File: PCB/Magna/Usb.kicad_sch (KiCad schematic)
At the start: 32 parts, among them J801 USB_A, J802 USB_C_Receptacle_USB2.0, J803 USB_B, U801 SRV05-4, U802 USB3300-EZK

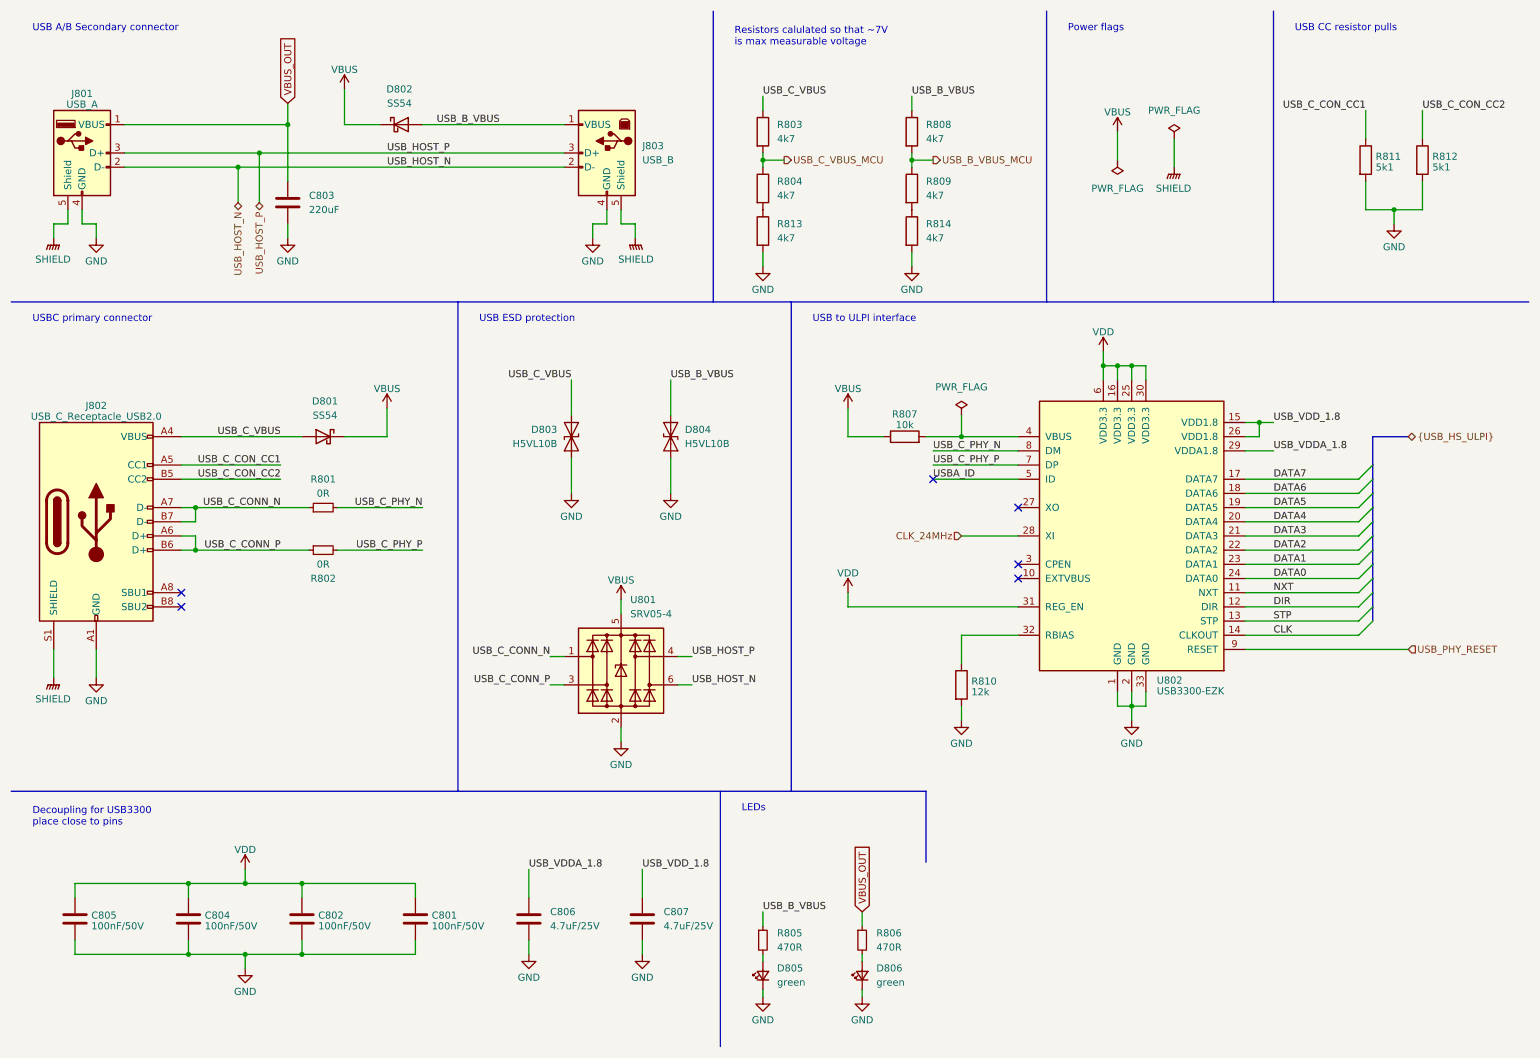
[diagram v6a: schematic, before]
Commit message: Split schematic to several projects
To allow for several boards to be done a kicad project
is needed for each
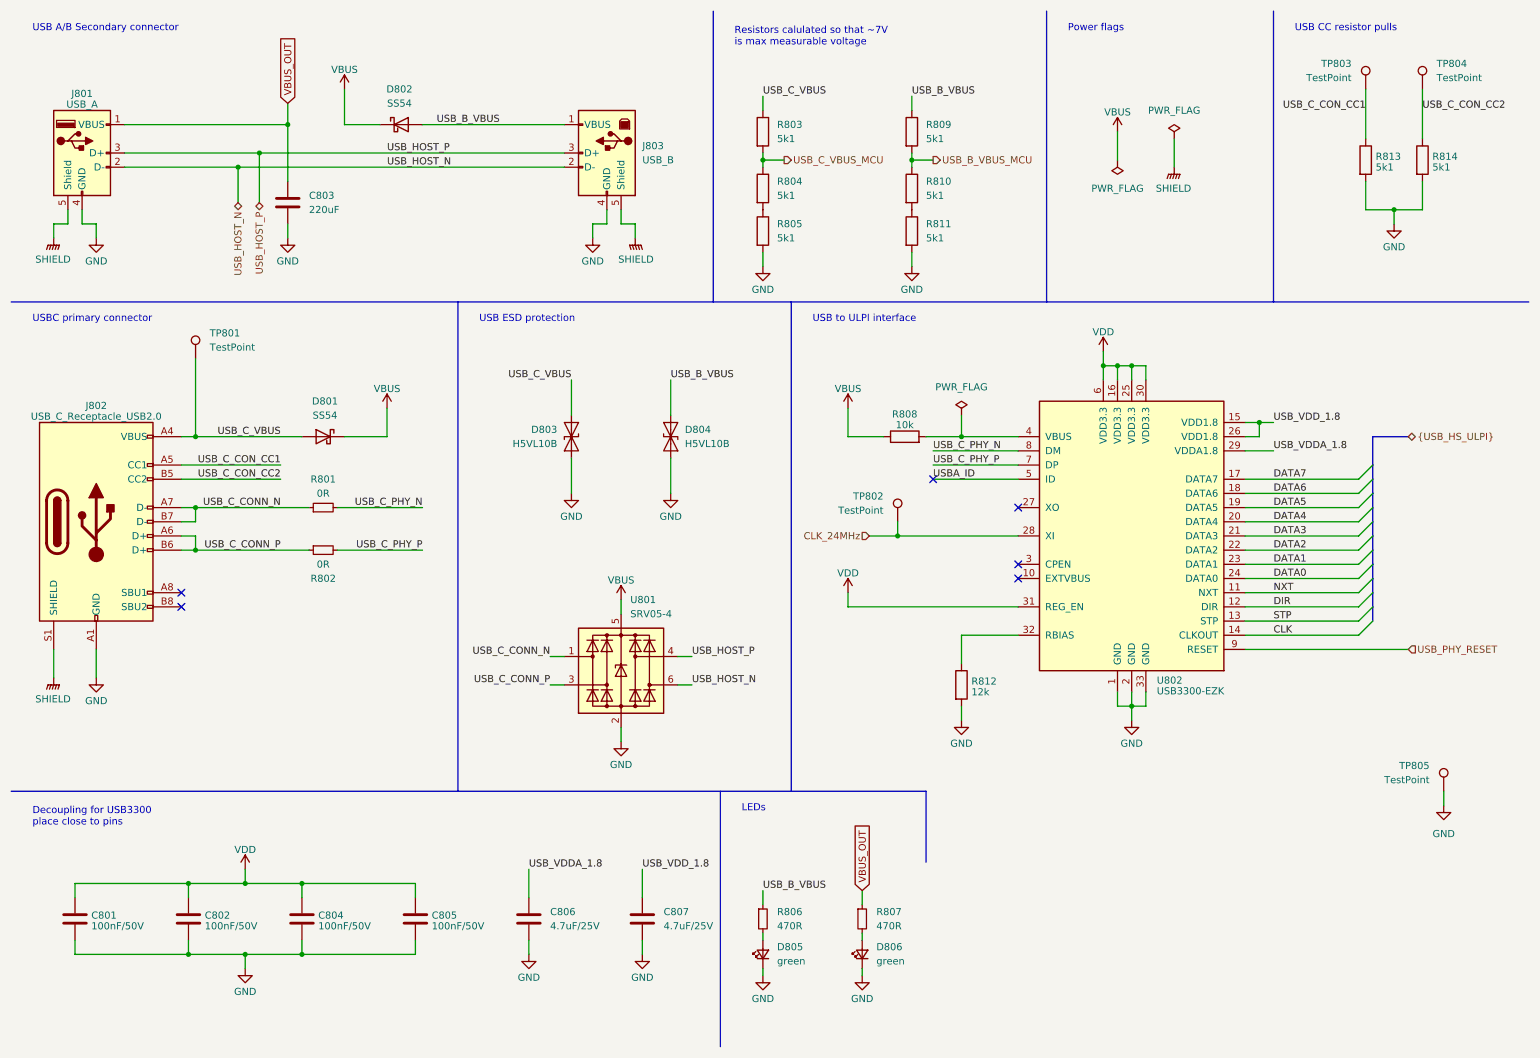
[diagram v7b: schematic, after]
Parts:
- added TP801, TP802, TP803, TP804, TP805: TestPoint, TestPoint:TestPoint_Keystone_5005-5009_Compact, symbol Connector:TestPoint
- R803, R804: value 4k7 -> 5k1; LCSC C17673 -> C218638
- R805: renamed from R813; value 4k7 -> 5k1; LCSC C17673 -> C218638
- R809: renamed from R808; value 4k7 -> 5k1; LCSC C17673 -> C218638
- R810: renamed from R809; value 4k7 -> 5k1; LCSC C17673 -> C218638
- R811: renamed from R814; value 4k7 -> 5k1; LCSC C17673 -> C218638
- renumbered C805 to C801, C804 to C802, C802 to C804, C801 to C805, R805 to R806, R806 to R807, R807 to R808, R810 to R812, R811 to R813, R812 to R814
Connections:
- net CLK_24MHz: now also TP802.1
- net GND: now also TP805.1
- net USB_C_CON_CC1: now also TP803.1
- net USB_C_CON_CC2: now also TP804.1
- net USB_C_VBUS: now also TP801.1
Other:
- moved on the sheet: D805, D806, R806, R807

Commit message: Change components on Main Board to use more of the same part#
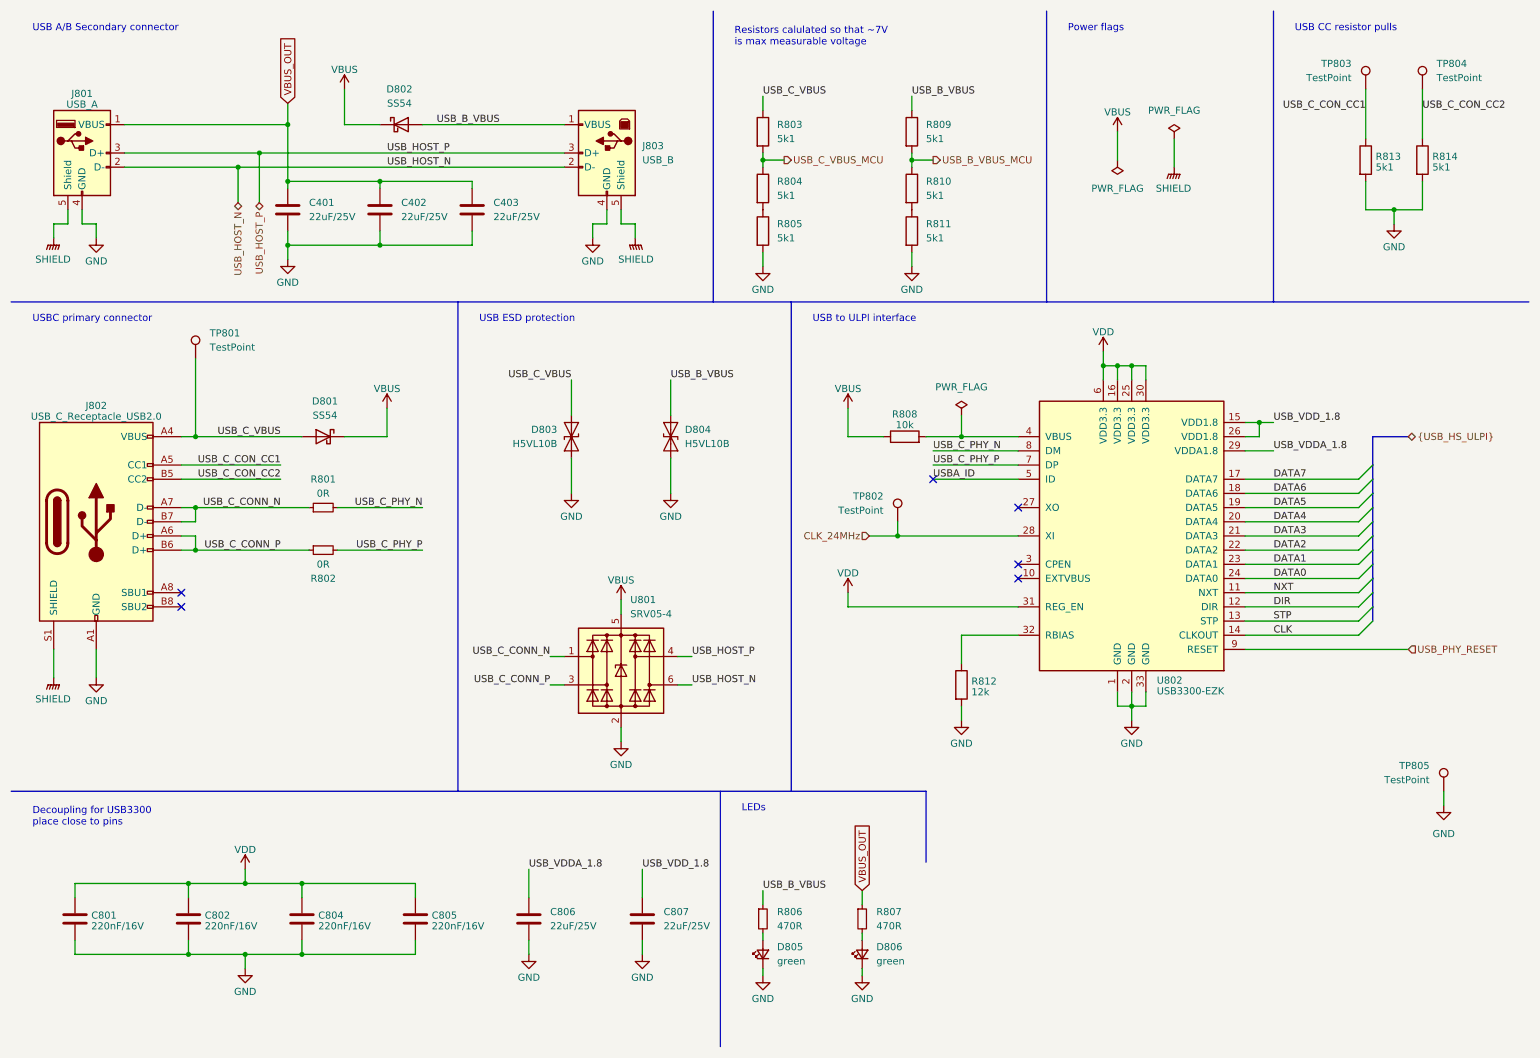
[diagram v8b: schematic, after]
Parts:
- removed C803: 220uF, Capacitor_SMD:CP_Elec_4x5.8, symbol Device:C
- added C401, C402, C403: 22uF/25V, Capacitor_SMD:C_0805_2012Metric_Pad1.18x1.45mm_HandSolder, symbol Device:C
- C801, C802, C804, C805: value 100nF/50V -> 220nF/16V; footprint Capacitor_SMD:C_0805_2012Metric_Pad1.18x1.45mm_HandSolder -> Capacitor_SMD:C_0402_1005Metric_Pad0.74x0.62mm_HandSolder; LCSC C49678 -> C16772
- C806, C807: value 4.7uF/25V -> 22uF/25V; LCSC C1779 -> C45783
- TP801, TP802, TP803, TP804, TP805: footprint TestPoint:TestPoint_Keystone_5005-5009_Compact -> TestPoint:TestPoint_Keystone_5000-5004_Miniature
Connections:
- net GND: now also C401.2, C402.2, C403.2
- net VBUS_OUT: now also C401.1, C402.1, C403.1
